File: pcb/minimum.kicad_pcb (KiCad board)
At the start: 2 copper layers, 55 x 50 mm, 23 parts, among them J1 USB4155-03-C_REVA, U1 RP2040, U2 SCD4x

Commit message: flash added
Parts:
- added U3: W25Q128JVPIM, SMD:W25Q128JVPIM, B.Cu at (99.9, 63.7)
- moved U1 2.90 mm to (99.9, 73.3)
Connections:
- C14 pad 2: Net-(U1-Pad20) -> Net-(C14-Pad2)
- R5 pad 2: Net-(U1-Pad21) -> Net-(R5-Pad2)
- U1 pad 20: (no net) -> Net-(C14-Pad2)
- U1 pad 21: (no net) -> Net-(R5-Pad2)

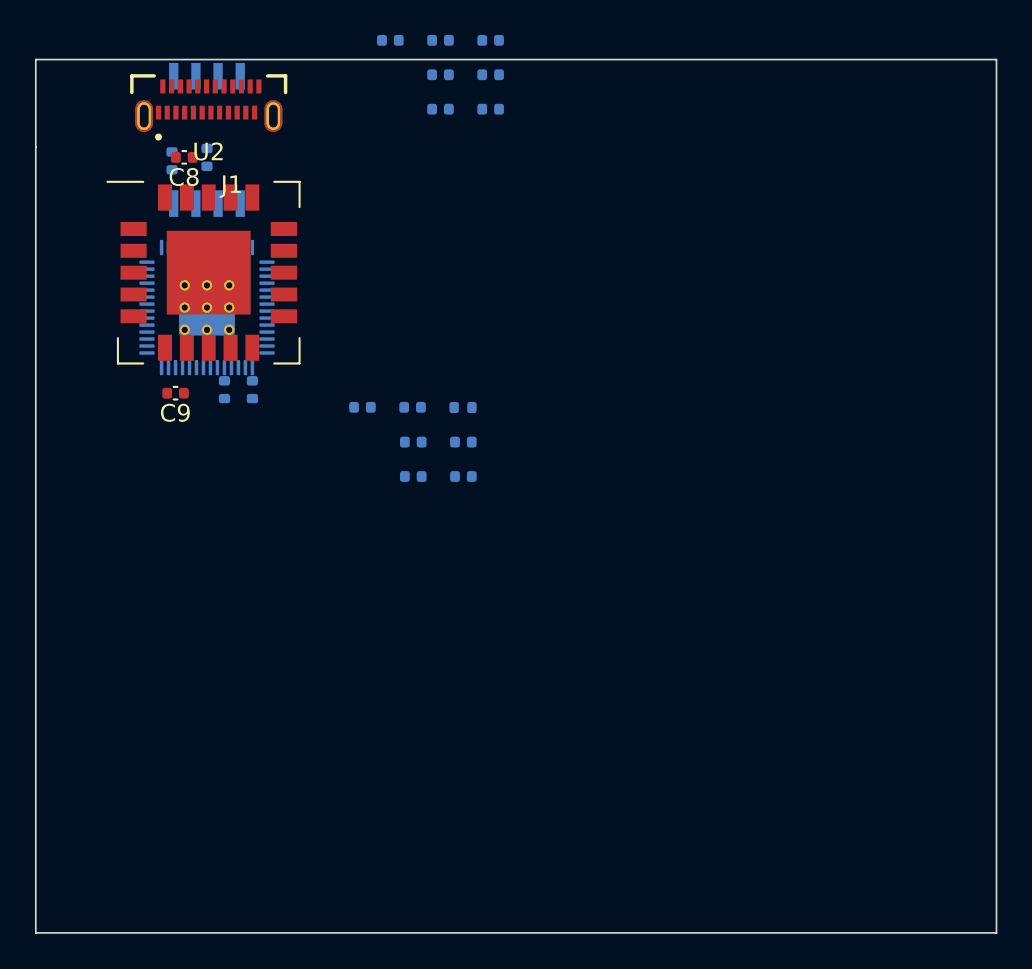
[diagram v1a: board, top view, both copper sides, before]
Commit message: connecting signals
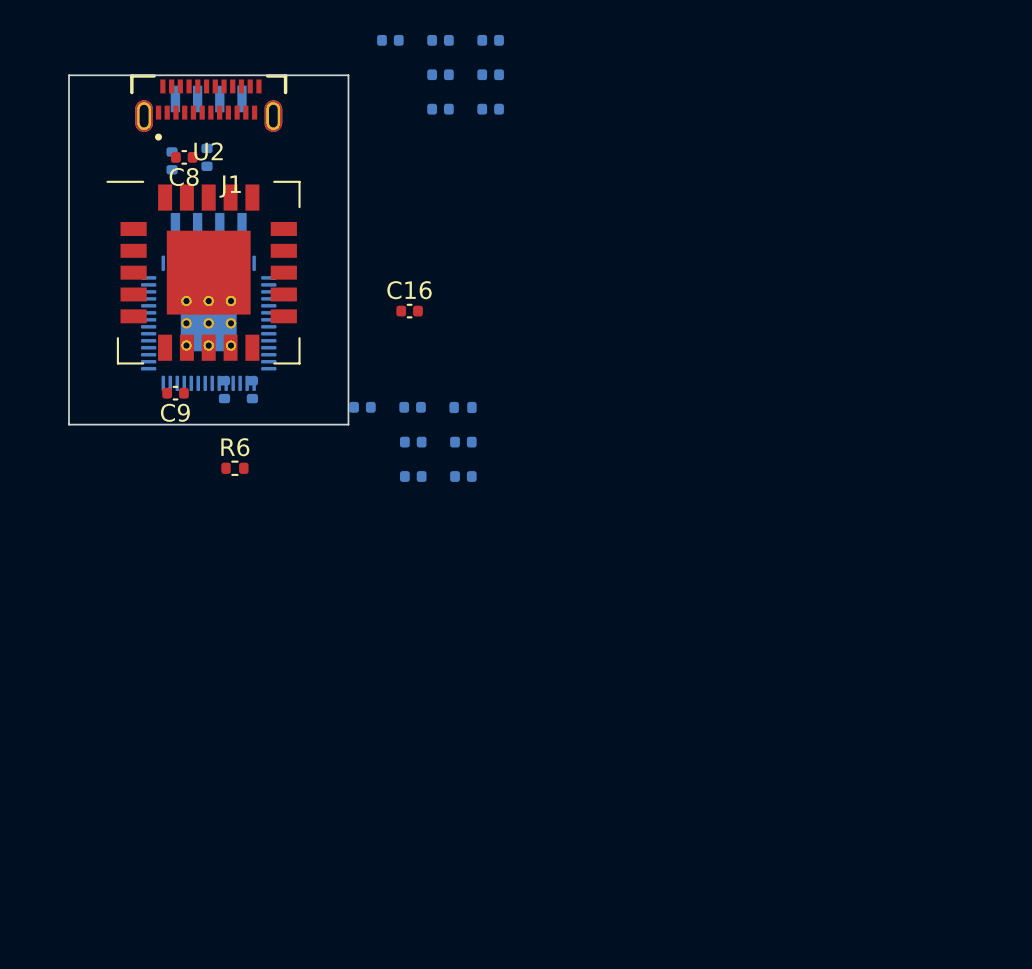
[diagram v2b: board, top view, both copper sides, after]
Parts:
- added C16: 100n, Capacitor_SMD:C_0402_1005Metric, F.Cu at (111.5, 73.5)
- added R6: 1k, Resistor_SMD:R_0402_1005Metric, F.Cu at (101.5, 82.5)
- moved U3 1.30 mm to (100.0, 65.0), turned to 90 degrees
- moved U1 0.91 mm to (100.0, 74.2)
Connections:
- J1 pad A6: Net-(J1-PadA6) -> /USB_D+
- J1 pad A7: Net-(J1-PadA7) -> /USB_D-
- J1 pad B6: (no net) -> /USB_D+
- J1 pad B7: (no net) -> /USB_D-
- R1 pad 1: Net-(J1-PadA6) -> /USB_D+
- R2 pad 2: Net-(J1-PadA7) -> /USB_D-
- U1 pad 19: (no net) -> GND
- U1 pad 51: (no net) -> /QSPI_SD3
- U1 pad 52: (no net) -> /QSPI_SCLK
- U1 pad 53: (no net) -> /QSPI_SD0
- U1 pad 54: (no net) -> /QSPI_SD2
- U1 pad 55: (no net) -> /QSPI_SD1
- U1 pad 56: (no net) -> /QSPI_SS
- U3 pad 1: unconnected-(U3-Pad1) -> /QSPI_SS
- U3 pad 2: unconnected-(U3-Pad2) -> /QSPI_SD1
- U3 pad 3: unconnected-(U3-Pad3) -> /QSPI_SD2
- U3 pad 5: unconnected-(U3-Pad5) -> /QSPI_SD0
- U3 pad 6: unconnected-(U3-Pad6) -> /QSPI_SCLK
- U3 pad 7: unconnected-(U3-Pad7) -> /QSPI_SD3
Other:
- board size 55 x 50 mm -> 16 x 20 mm

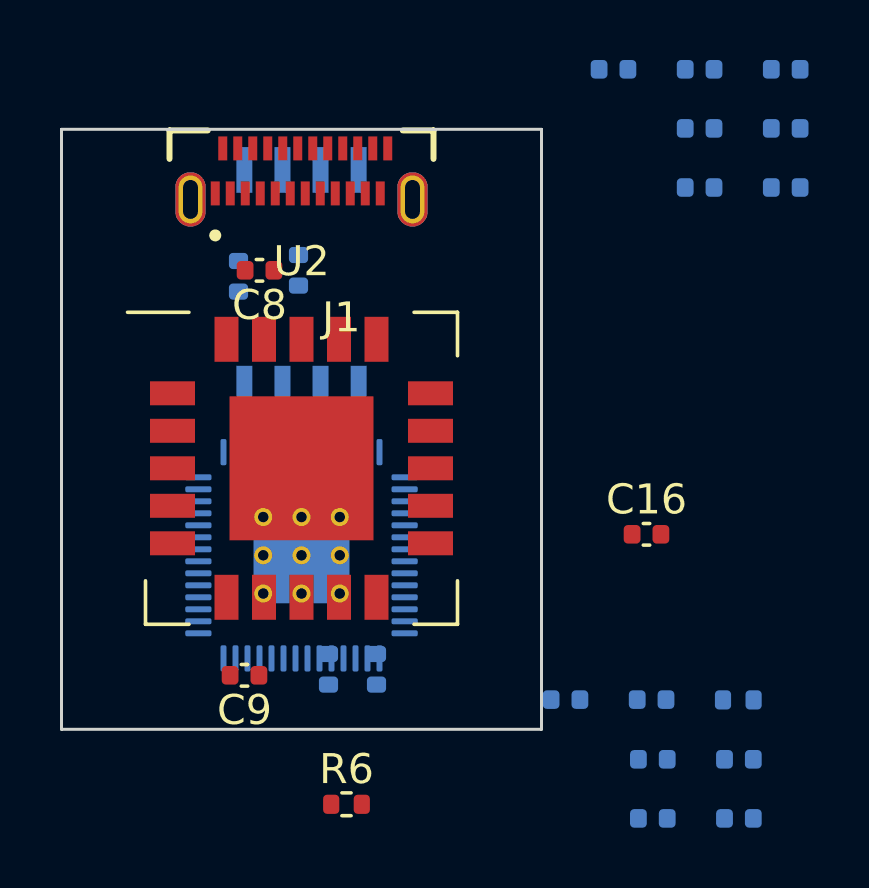
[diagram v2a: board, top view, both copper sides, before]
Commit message: connecting signals
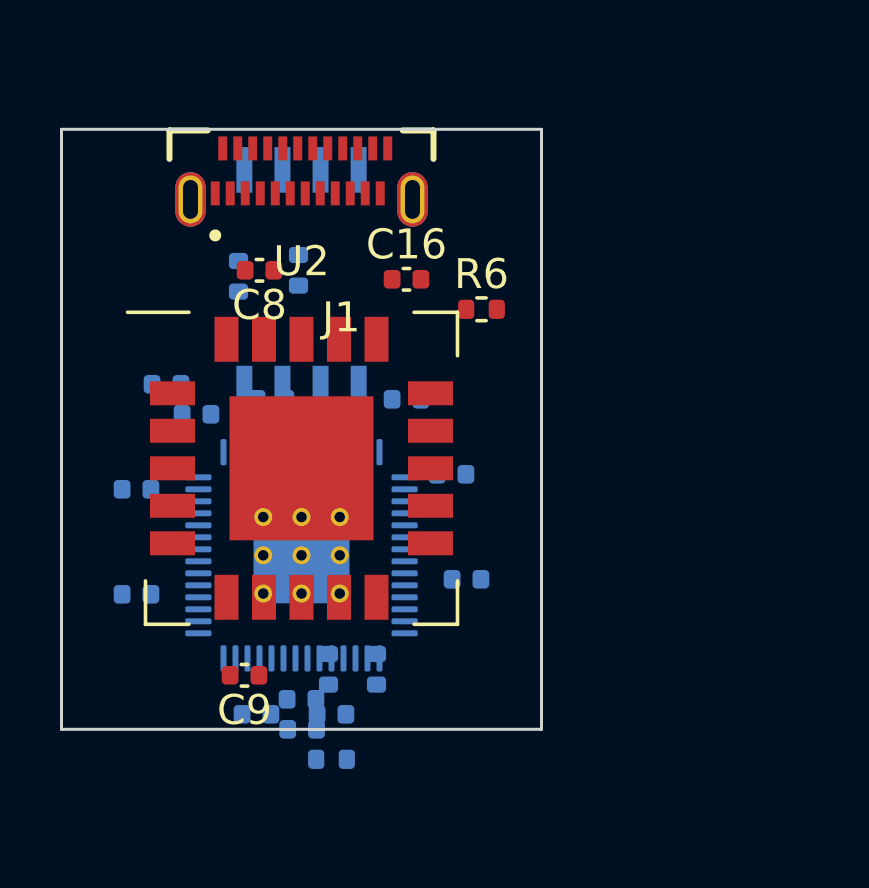
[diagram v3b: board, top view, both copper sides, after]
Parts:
- moved C2 25.5 mm to (94.5, 75.5)
- moved C5 24.8 mm to (101.0, 79.5)
- moved C7 22.3 mm to (95.5, 68.5)
- moved C10 21.4 mm to (96.5, 69.5)
- moved C1 21.2 mm to (94.5, 72.0)
- moved C6 19.3 mm to (101.0, 70.0)
- moved C11 17.5 mm to (99.0, 69.0)
- moved R6 17.1 mm to (106.0, 66.0)
- moved C4 16.9 mm to (105.5, 75.0)
- moved C13 16.5 mm to (98.5, 79.5)
- moved R5 13.7 mm to (101.0, 81.0)
- moved C3 12.6 mm to (105.0, 71.5)
- moved C15 12.1 mm to (100.0, 80.0)
- moved C16 11.7 mm to (103.5, 65.0)
- moved C14 11.7 mm to (100.0, 79.0)
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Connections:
- R6 pad 1: Net-(J2-Pad2) -> (no net)
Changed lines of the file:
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@@
   (net 22 "/USB_D+")
   (net 23 "/USB_D-")
-  (net 24 "Net-(J2-Pad2)")
   (footprint "SMD:QFN-20_EP_10.1x10.1_Pitch1.25mm" (layer "F.Cu")
     (at 100 71.3)
@@
   )
   (footprint "Resistor_SMD:R_0402_1005Metric" (layer "F.Cu")
-    (at 101.5 82.5)
+    (at 106 66)
     (descr "Resistor SMD 0402 (1005 Metric), square (rectangular) end terminal, IPC_7351 nominal, (Body size source: IPC-SM-782 page 72, https://www.pcb-3d.com/wordpress/wp-content/uploads/ipc-sm-782a_amendment_1_and_2.pdf), generated with kicad-footprint-generator")
     (tags "resistor")
@@
     (fp_line (start -0.525 -0.27) (end 0.525 -0.27) (layer "F.Fab") (width 0.1))
     (pad "1" smd roundrect locked (at -0.51 0) (size 0.54 0.64) (layers "F.Cu" "F.Paste" "F.Mask") (roundrect_rratio 0.25)
-      (net 24 "Net-(J2-Pad2)") (pintype "passive"))
+      (pintype "passive"))
     (pad "2" smd roundrect locked (at 0.51 0) (size 0.54 0.64) (layers "F.Cu" "F.Paste" "F.Mask") (roundrect_rratio 0.25)
       (net 21 "/QSPI_SS") (pintype "passive"))
@@
   )
   (footprint "Capacitor_SMD:C_0402_1005Metric" (layer "F.Cu")
-    (at 111.5 73.5)
+    (at 103.5 65)
     (descr "Capacitor SMD 0402 (1005 Metric), square (rectangular) end terminal, IPC_7351 nominal, (Body size source: IPC-SM-782 page 76, https://www.pcb-3d.com/wordpress/wp-content/uploads/ipc-sm-782a_amendment_1_and_2.pdf), generated with kicad-footprint-generator")
     (tags "capacitor")
@@
   )
   (footprint "Capacitor_SMD:C_0402_1005Metric" (layer "B.Cu")
-    (at 111.71 82.97 180)
+    (at 100.02 80 180)
     (descr "Capacitor SMD 0402 (1005 Metric), square (rectangular) end terminal, IPC_7351 nominal, (Body size source: IPC-SM-782 page 76, https://www.pcb-3d.com/wordpress/wp-content/uploads/ipc-sm-782a_amendment_1_and_2.pdf), generated with kicad-footprint-generator")
     (tags "capacitor")
@@
   )
   (footprint "Capacitor_SMD:C_0402_1005Metric" (layer "B.Cu")
-    (at 116.14 59.97 180)
+    (at 95.5 68.5 180)
     (descr "Capacitor SMD 0402 (1005 Metric), square (rectangular) end terminal, IPC_7351 nominal, (Body size source: IPC-SM-782 page 76, https://www.pcb-3d.com/wordpress/wp-content/uploads/ipc-sm-782a_amendment_1_and_2.pdf), generated with kicad-footprint-generator")
     (tags "capacitor")
@@
   )
   (footprint "Capacitor_SMD:C_0402_1005Metric" (layer "B.Cu")
-    (at 114.58 81 180)
+    (at 96.5 69.5 180)
     (descr "Capacitor SMD 0402 (1005 Metric), square (rectangular) end terminal, IPC_7351 nominal, (Body size source: IPC-SM-782 page 76, https://www.pcb-3d.com/wordpress/wp-content/uploads/ipc-sm-782a_amendment_1_and_2.pdf), generated with kicad-footprint-generator")
     (tags "capacitor")
@@
     (fp_line (start 0.5 -0.25) (end -0.5 -0.25) (layer "B.Fab") (width 0.1))
     (pad "1" smd roundrect locked (at -0.48 0 180) (size 0.56 0.62) (layers "B.Cu" "B.Paste" "B.Mask") (roundrect_rratio 0.25)
-      (net 4 "+3V3") (pintype "passive"))
+      (net 4 "+3V3"))
     (pad "2" smd roundrect locked (at 0.48 0 180) (size 0.56 0.62) (layers "B.Cu" "B.Paste" "B.Mask") (roundrect_rratio 0.25)
-      (net 5 "GND") (pintype "passive"))
+      (net 5 "GND"))
     (model "${KISYS3DMOD}/Capacitor_SMD.3dshapes/C_0402_1005Metric.wrl"
       (offset (xyz 0 0 0))
@@
   )
   (footprint "Capacitor_SMD:C_0402_1005Metric" (layer "B.Cu")
-    (at 111.71 81 180)
+    (at 99 69 180)
     (descr "Capacitor SMD 0402 (1005 Metric), square (rectangular) end terminal, IPC_7351 nominal, (Body size source: IPC-SM-782 page 76, https://www.pcb-3d.com/wordpress/wp-content/uploads/ipc-sm-782a_amendment_1_and_2.pdf), generated with kicad-footprint-generator")
     (tags "capacitor")
@@
   )
   (footprint "Capacitor_SMD:C_0402_1005Metric" (layer "B.Cu")
-    (at 111.67 79.01 180)
+    (at 100 79 180)
     (descr "Capacitor SMD 0402 (1005 Metric), square (rectangular) end terminal, IPC_7351 nominal, (Body size source: IPC-SM-782 page 76, https://www.pcb-3d.com/wordpress/wp-content/uploads/ipc-sm-782a_amendment_1_and_2.pdf), generated with kicad-footprint-generator")
     (tags "capacitor")
@@
   )
   (footprint "Capacitor_SMD:C_0402_1005Metric" (layer "B.Cu")
-    (at 110.4 58 180)
+    (at 94.5 72 180)
     (descr "Capacitor SMD 0402 (1005 Metric), square (rectangular) end terminal, IPC_7351 nominal, (Body size source: IPC-SM-782 page 76, https://www.pcb-3d.com/wordpress/wp-content/uploads/ipc-sm-782a_amendment_1_and_2.pdf), generated with kicad-footprint-generator")
     (tags "capacitor")
@@
   )
   (footprint "Resistor_SMD:R_0402_1005Metric" (layer "B.Cu")
-    (at 114.56 79.02 180)
+    (at 101 81 180)
     (descr "Resistor SMD 0402 (1005 Metric), square (rectangular) end terminal, IPC_7351 nominal, (Body size source: IPC-SM-782 page 72, https://www.pcb-3d.com/wordpress/wp-content/uploads/ipc-sm-782a_amendment_1_and_2.pdf), generated with kicad-footprint-generator")
     (tags "resistor")
@@
   )
   (footprint "Capacitor_SMD:C_0402_1005Metric" (layer "B.Cu")
-    (at 108.8 79.01 180)
+    (at 103.5 69 180)
     (descr "Capacitor SMD 0402 (1005 Metric), square (rectangular) end terminal, IPC_7351 nominal, (Body size source: IPC-SM-782 page 76, https://www.pcb-3d.com/wordpress/wp-content/uploads/ipc-sm-782a_amendment_1_and_2.pdf), generated with kicad-footprint-generator")
     (tags "capacitor")
@@
   )
   (footprint "Capacitor_SMD:C_0402_1005Metric" (layer "B.Cu")
-    (at 116.14 61.94 180)
+    (at 94.5 75.5 180)
     (descr "Capacitor SMD 0402 (1005 Metric), square (rectangular) end terminal, IPC_7351 nominal, (Body size source: IPC-SM-782 page 76, https://www.pcb-3d.com/wordpress/wp-content/uploads/ipc-sm-782a_amendment_1_and_2.pdf), generated with kicad-footprint-generator")
     (tags "capacitor")
@@
   )
   (footprint "Capacitor_SMD:C_0402_1005Metric" (layer "B.Cu")
-    (at 113.27 61.94 180)
+    (at 105 71.5 180)
     (descr "Capacitor SMD 0402 (1005 Metric), square (rectangular) end terminal, IPC_7351 nominal, (Body size source: IPC-SM-782 page 76, https://www.pcb-3d.com/wordpress/wp-content/uploads/ipc-sm-782a_amendment_1_and_2.pdf), generated with kicad-footprint-generator")
     (tags "capacitor")
@@
   )
   (footprint "Capacitor_SMD:C_0402_1005Metric" (layer "B.Cu")
-    (at 113.27 59.97 180)
+    (at 105.5 75 180)
     (descr "Capacitor SMD 0402 (1005 Metric), square (rectangular) end terminal, IPC_7351 nominal, (Body size source: IPC-SM-782 page 76, https://www.pcb-3d.com/wordpress/wp-content/uploads/ipc-sm-782a_amendment_1_and_2.pdf), generated with kicad-footprint-generator")
     (tags "capacitor")
@@
   )
   (footprint "Capacitor_SMD:C_0402_1005Metric" (layer "B.Cu")
-    (at 114.58 82.97 180)
+    (at 98.5 79.5 180)
     (descr "Capacitor SMD 0402 (1005 Metric), square (rectangular) end terminal, IPC_7351 nominal, (Body size source: IPC-SM-782 page 76, https://www.pcb-3d.com/wordpress/wp-content/uploads/ipc-sm-782a_amendment_1_and_2.pdf), generated with kicad-footprint-generator")
     (tags "capacitor")
@@
   )
   (footprint "Capacitor_SMD:C_0402_1005Metric" (layer "B.Cu")
-    (at 116.14 58 180)
+    (at 101 70 180)
     (descr "Capacitor SMD 0402 (1005 Metric), square (rectangular) end terminal, IPC_7351 nominal, (Body size source: IPC-SM-782 page 76, https://www.pcb-3d.com/wordpress/wp-content/uploads/ipc-sm-782a_amendment_1_and_2.pdf), generated with kicad-footprint-generator")
     (tags "capacitor")
@@
   )
   (footprint "Capacitor_SMD:C_0402_1005Metric" (layer "B.Cu")
-    (at 113.27 58 180)
+    (at 101 79.5 180)
     (descr "Capacitor SMD 0402 (1005 Metric), square (rectangular) end terminal, IPC_7351 nominal, (Body size source: IPC-SM-782 page 76, https://www.pcb-3d.com/wordpress/wp-content/uploads/ipc-sm-782a_amendment_1_and_2.pdf), generated with kicad-footprint-generator")
     (tags "capacitor")

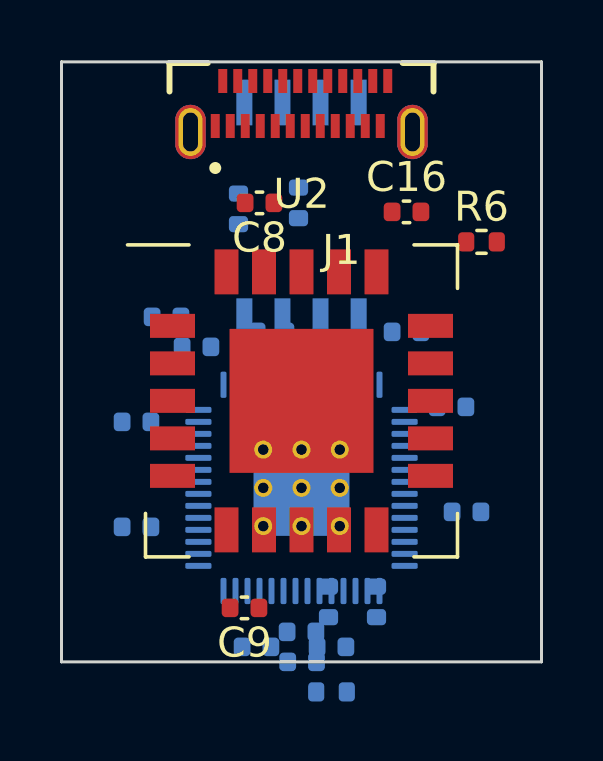
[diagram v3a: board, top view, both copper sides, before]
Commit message: flash changed due to space constrains
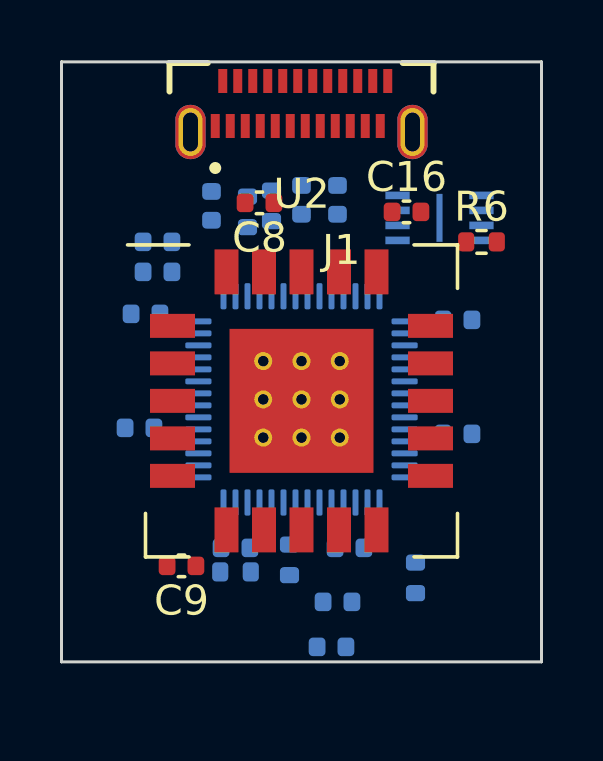
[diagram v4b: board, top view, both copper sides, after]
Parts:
- U3: value W25Q128JVPIM -> W25Q16JVUXIQ; footprint SMD:W25Q128JVPIM -> SMD:W25Q16JVUXIQ
- moved C6 5.49 mm to (100.0, 64.6), turned to 90 degrees
- moved C12 4.96 mm to (101.2, 64.6), turned to 90 degrees
- moved C11 4.65 mm to (97.0, 64.8), turned to 90 degrees
- moved R5 4.62 mm to (99.6, 76.6), turned to 90 degrees
- moved U3 4.60 mm to (104.6, 65.2), turned to 180 degrees
- moved C10 3.73 mm to (95.2, 66.0)
- moved C1 3.61 mm to (94.8, 68.4)
- moved C13 3.37 mm to (97.8, 76.2)
- moved C2 3.30 mm to (94.6, 72.2)
- moved R3 3.26 mm to (97.8, 77.0), turned to 180 degrees
- moved C14 3.22 mm to (101.6, 76.2)
- moved U1 2.95 mm to (100.0, 71.2)
- moved C3 2.91 mm to (105.2, 68.6), turned to 0 degrees
- moved C4 2.62 mm to (105.2, 72.4), turned to 0 degrees
- moved C9 2.52 mm to (96.0, 76.8)
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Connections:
- net Net-(C14-Pad2) renamed /XIN
- net Net-(C15-Pad2) renamed /XOUTc
- net Net-(R5-Pad2) renamed /XOUT
